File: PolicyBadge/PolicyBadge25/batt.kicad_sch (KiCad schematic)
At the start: 6 parts, among them U2 SGM40567-4.2XG/TR

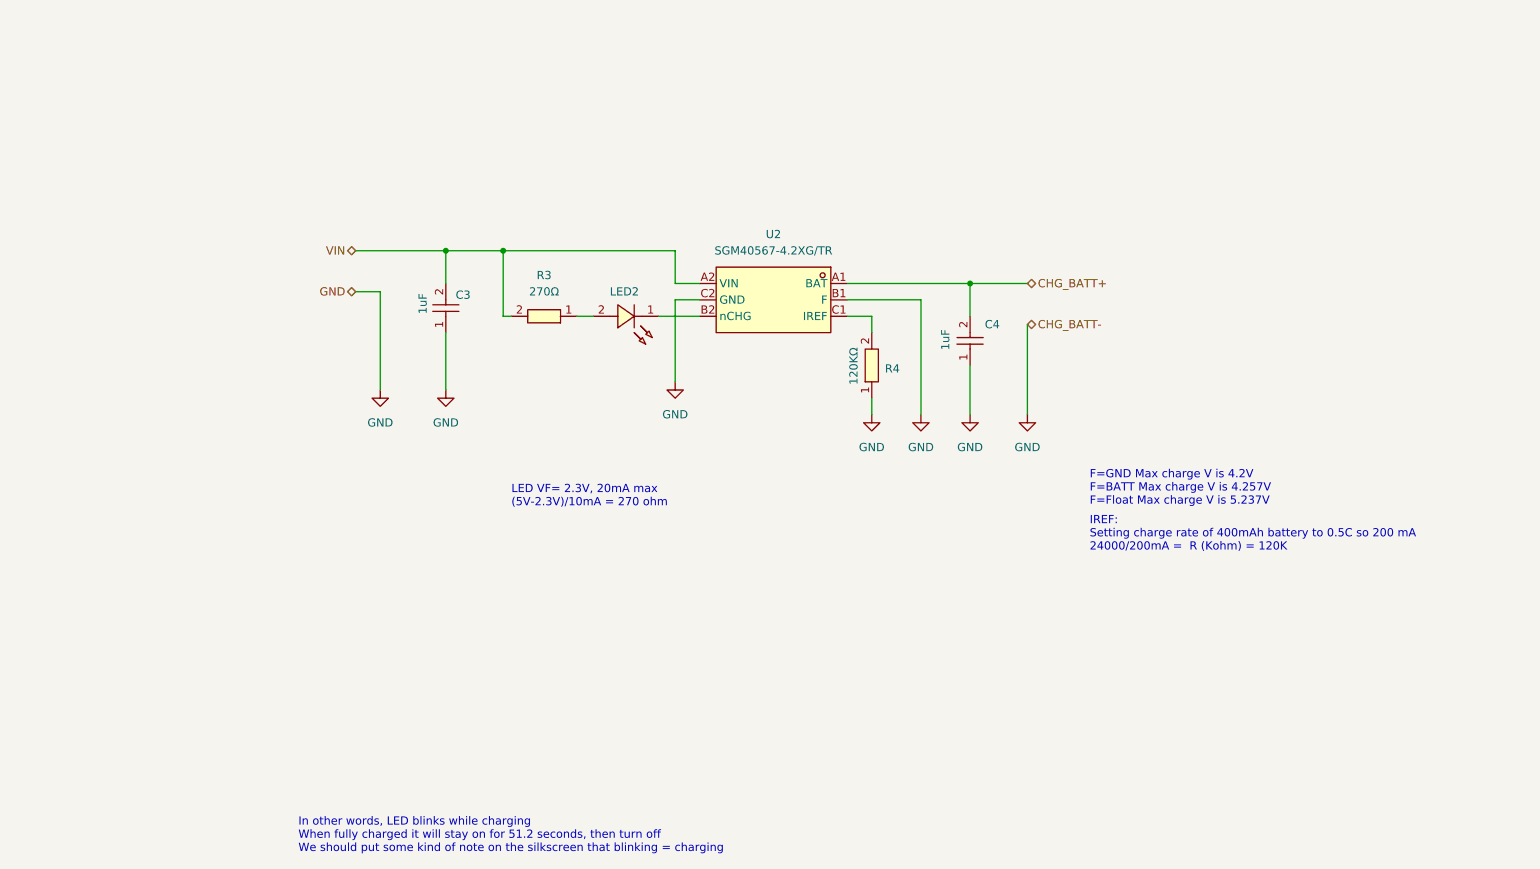
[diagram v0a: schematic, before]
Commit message: Use IP2312 battery management ic
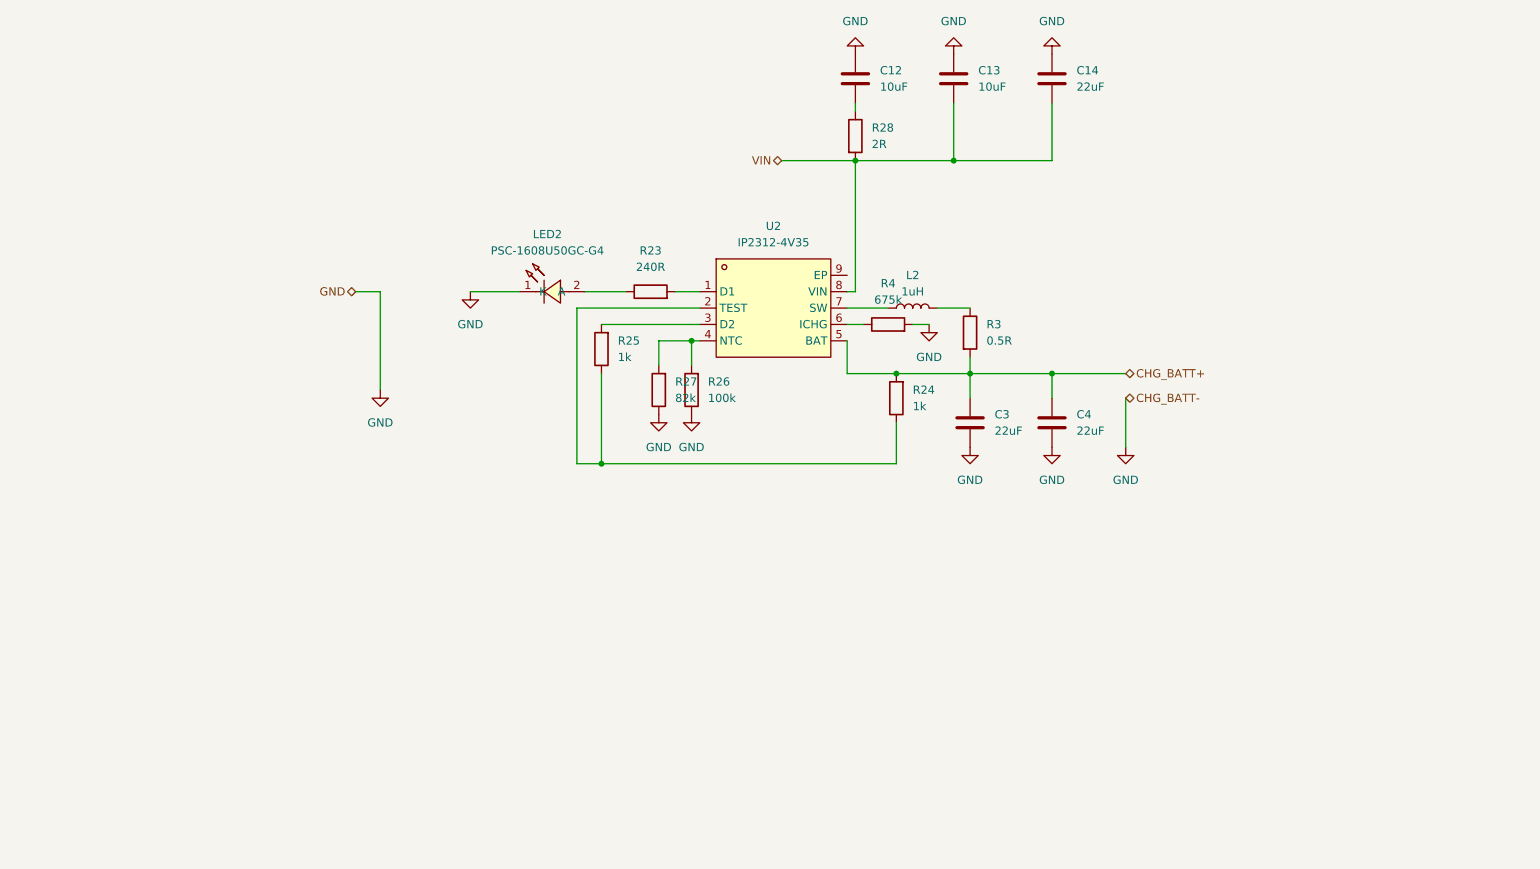
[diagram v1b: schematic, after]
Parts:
- removed C3, C4: 1uF, imported:C0603, symbol JLCPCB:CL10A105KO8NNNC
- removed LED2: ~, imported:LED0603-RD_RED, symbol JLCPCB:XL-1608SURC-06
- removed R3: 270Ω, imported:R0603, symbol JLCPCB:0603WAF2700T5E
- removed R4: 120KΩ, imported:R0603, symbol JLCPCB:0603WAF1203T5E
- removed U2: SGM40567-4.2XG/TR, imported:WLCSP-6_L1.2-W0.9-R3-C2-P0.40-TL, symbol JLCPCB:SGM40567-4.2XG_TR
- added C12, C13: 10uF, symbol Device:C
- added C14, C3, C4: 22uF, symbol Device:C
- added L2: 1uH, symbol Device:L
- added LED2: PSC-1608U50GC-G4, easyeda2kicad:LED0603-RD_GREEN, symbol easyeda2kicad:PSC-1608U50GC-G4
- added R23: 240R, symbol Device:R
- added R24, R25: 1k, symbol Device:R
- added R26: 100k, symbol Device:R
- added R27: 82k, symbol Device:R
- added R28: 2R, symbol Device:R
- added R3: 0.5R, symbol Device:R
- added R4: 675k, symbol Device:R
- added U2: IP2312-4V35, easyeda2kicad:ESOP-8_L4.9-W3.9-P1.27-LS6.0-BL-EP, symbol easyeda2kicad:IP2312-4V35
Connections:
- net CHG_BATT+: now also C3.1, C4.1, R24.2, R3.2, U2.5 (BAT)
- net GND: now also C12.1, C13.1, C14.1, C3.2, C4.2, LED2.1 (K), R26.1, R27.1, R4.2
- net VIN: now also C13.2, C14.2, R28.2, U2.8 (VIN)
- new net: R23.2, U2.1 (D1)
- new net: R24.1, R25.1, U2.2 (TEST)
- new net: R25.2, U2.3 (D2)
- new net: R26.2, R27.2, U2.4 (NTC)
- new net: R4.1, U2.6 (ICHG)
- new net: L2.1, U2.7 (SW)
- new net: LED2.2 (A), R23.1
- new net: C12.2, R28.1
- new net: L2.2, R3.1
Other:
- note removed: "F=GND Max charge V is 4.2V F=BATT Max charge V is 4.257V F=Float Max charge V is 5.237V"
- note removed: "IREF: Setting charge rate of 400mAh battery to 0.5C so 200 mA 24000/200mA = R (Kohm) = 120K"
- note removed: "In other words, LED blinks while charging When fully charged it will stay on for 51.2 seconds, then turn off We should put some kind of note on the silkscreen that blinking = charging"
- note removed: "LED VF= 2.3V, 20mA max (5V-2.3V)/10mA = 270 ohm"

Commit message: Released version of PCB
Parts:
- removed C12, C13: 10uF, symbol Device:C
- removed C14, C3, C4: 22uF, symbol Device:C
- removed L2: 1uH, symbol Device:L
- removed LED2: PSC-1608U50GC-G4, easyeda2kicad:LED0603-RD_GREEN, symbol easyeda2kicad:PSC-1608U50GC-G4
- removed R23: 240R, symbol Device:R
- removed R24, R25: 1k, symbol Device:R
- removed R26: 100k, symbol Device:R
- removed R27: 82k, symbol Device:R
- removed R28: 2R, symbol Device:R
- removed R3: 0.5R, symbol Device:R
- removed R4: 675k, symbol Device:R
- removed U2: IP2312-4V35, easyeda2kicad:ESOP-8_L4.9-W3.9-P1.27-LS6.0-BL-EP, symbol easyeda2kicad:IP2312-4V35
- added C13, C14: 10uF, imported:C0603, symbol JLCPCB:GRM188R6YA106MA73D
- added C15, C16, C17: 22uF, imported:C0805, symbol JLCPCB:CL21A226MAYNNNE
- added L2: 1uH, imported:L2520, symbol JLCPCB:DFE252012F-1R0M=P2
- added LED5: ~, imported:LED0603-RD_GREEN, symbol JLCPCB:PSC-1608U50GC-G4
- added R10: 51kΩ, imported:R0603, symbol JLCPCB:0603WAF5102T5E
- added R11: 680kΩ, imported:R0603, symbol JLCPCB:0603WAF6803T5E
- added R12: 0.5Ω, imported:R0603, symbol JLCPCB:0603WAF500LT5E
- added R7: 240Ω, imported:R0603, symbol JLCPCB:0603WAF2400T5E
- added R8, R9: 1KΩ, imported:R0603, symbol JLCPCB:0603WAF1001T5E
- added U11: IP2312-4V35, imported:ESOP-8_L4.9-W3.9-P1.27-LS6.0-BL-EP, symbol JLCPCB:IP2312-4V35
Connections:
- net CHG_BATT+: now also C17.2, L2.2, R12.2, R8.1, R9.2
- net GND: now also C13.1, C14.1, C15.1, C16.1, C17.1, LED5.1 (K), R10.1, R11.1, U11.9 (EP)
- net VIN: now also C13.2, C14.2, C15.2, U11.8 (VIN)
- new net: R10.2, U11.4 (NTC)
- new net: C16.2, R12.1, U11.5 (BAT)
- new net: R11.2, U11.6 (ICHG)
- new net: R8.2, U11.3 (D2)
- new net: L2.1, U11.7 (SW)
- new net: R9.1, U11.2 (TEST)
- new net: LED5.2 (A), R7.1
- new net: R7.2, U11.1 (D1)
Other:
- note added: "Battery type set to LiPoly with 4.2V by not connecting an RVSET resistor"
- note added: "ICHG resistor set to: 135000/680000 = 199 mA"
- note added: "One light mode configured"

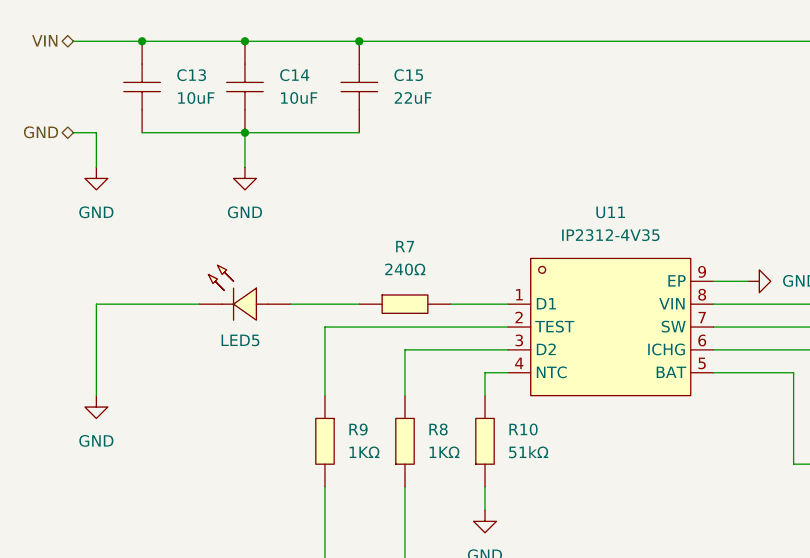
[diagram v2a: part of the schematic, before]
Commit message: Added batt monitoring
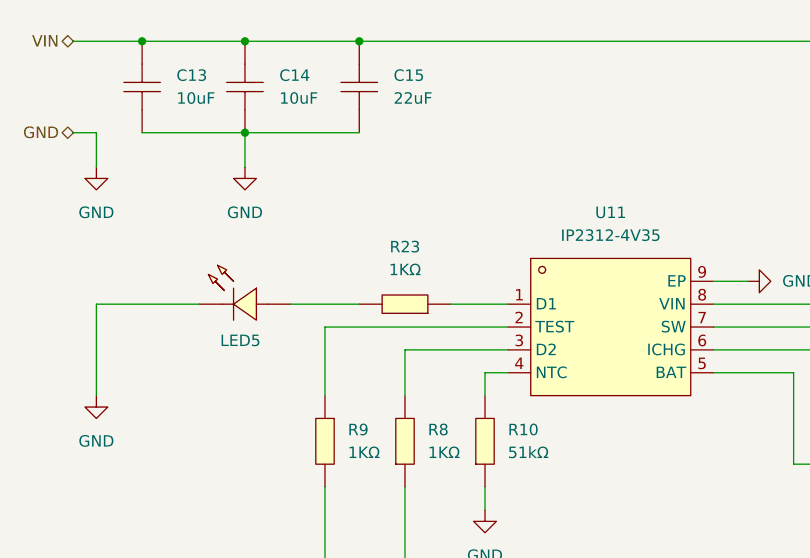
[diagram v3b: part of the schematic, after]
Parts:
- removed R7: 240Ω, imported:R0603, symbol JLCPCB:0603WAF2400T5E
- added R23: 1KΩ, imported:R0603, symbol JLCPCB:0603WAF1001T5E
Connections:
- net at LED5.2 (A): now also R23.2
- net at U11.1 (D1): now also R23.1
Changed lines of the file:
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@@
+	)
+	(symbol
+		(lib_id "JLCPCB:0603WAF1001T5E")
+		(at 115.57 86.36 180)
+		(unit 1)
+		(exclude_from_sim no)
+		(in_bom yes)
+		(on_board yes)
+		(dnp no)
+		(fields_autoplaced yes)
+		(property "Reference" "R23"
+			(at 115.57 80.01 0)
+			(effects
+				(font
+					(size 1.27 1.27)
+				)
+			)
+		)
+		(property "Value" "1KΩ"
+			(at 115.57 82.55 0)
+			(effects
+				(font
+					(size 1.27 1.27)
+				)
+			)
+		)
+		(property "Footprint" "imported:R0603"
+			(at 115.57 78.74 0)
+			(effects
+				(font
+					(size 1.27 1.27)
+				)
+				(hide yes)
+			)
+		)
+		(property "Datasheet" "https://lcsc.com/product-detail/Chip-Resistor-Surface-Mount-UniOhm_1KR-1001-1_C21190.html"
+			(at 115.57 76.2 0)
+			(effects
+				(font
+					(size 1.27 1.27)
+				)
+				(hide yes)
+			)
+		)
+		(property "Description" ""
+			(at 115.57 86.36 0)
+			(effects
+				(font
+					(size 1.27 1.27)
+				)
+				(hide yes)
+			)
+		)
+		(property "LCSC Part" "C21190"
+			(at 115.57 73.66 0)
+			(effects
+				(font
+					(size 1.27 1.27)
+				)
+				(hide yes)
+			)
+		)
+		(property "MPN" "0603WAF1001T5E"
+			(at 115.57 86.36 0)
+			(effects
+				(font
+					(size 1.27 1.27)
+				)
+				(hide yes)
+			)
+		)
+		(pin "2"
+		)
+		(pin "1"
+		)
+		(instances
+			(project "PolicyBadge25"
+				(path "/3911717a-8f19-42c2-8f04-ebfae4e12db6/9ee4cd69-77a2-45d3-80ac-b404a76d79db"
+					(reference "R23")
+					(unit 1)
+				)
+			)
+		)
 	)
 	(symbol
@@
 					(unit 1)
 				)
-			)
-		)
-	)
-	(symbol
-		(lib_id "JLCPCB:0603WAF2400T5E")
-		(at 115.57 86.36 0)
-		(unit 1)
-		(exclude_from_sim no)
-		(in_bom yes)
-		(on_board yes)
-		(dnp no)
-		(fields_autoplaced yes)
-		(property "Reference" "R7"
-			(at 115.57 80.01 0)
-			(effects
-				(font
-					(size 1.27 1.27)
-				)
-			)
-		)
-		(property "Value" "240Ω"
-			(at 115.57 82.55 0)
-			(effects
-				(font
-					(size 1.27 1.27)
-				)
-			)
-		)
-		(property "Footprint" "imported:R0603"
-			(at 115.57 93.98 0)
-			(effects
-				(font
-					(size 1.27 1.27)
-				)
-				(hide yes)
-			)
-		)
-		(property "Datasheet" "https://lcsc.com/product-detail/Chip-Resistor-Surface-Mount-UniOhm_240R-2400-1_C23350.html"
-			(at 115.57 96.52 0)
-			(effects
-				(font
-					(size 1.27 1.27)
-				)
-				(hide yes)
-			)
-		)
-		(property "Description" ""
-			(at 115.57 86.36 0)
-			(effects
-				(font
-					(size 1.27 1.27)
-				)
-				(hide yes)
-			)
-		)
-		(property "LCSC Part" "C23350"
-			(at 115.57 99.06 0)
-			(effects
-				(font
-					(size 1.27 1.27)
-				)
-				(hide yes)
-			)
-		)
-		(property "MPN" "0603WAF2400T5E"
-			(at 115.57 86.36 0)
-			(effects
-				(font
-					(size 1.27 1.27)
-				)
-				(hide yes)
-			)
-		)
-		(pin "2"
-		)
-		(pin "1"
-		)
-		(instances
-			(project "PolicyBadge25"
-				(path "/3911717a-8f19-42c2-8f04-ebfae4e12db6/9ee4cd69-77a2-45d3-80ac-b404a76d79db"
-					(reference "R7")
-					(unit 1)
-				)

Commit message: Lots of changes, laying out board for board shape
Updated switches
Added headers for XAIO
Fixed Batt Connector polarity
10K pullup on int
Batt monitor resistor divider
Fix buzzer trace
XAIO footprint spacing
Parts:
- renumbered C15 to C1, C13 to C2, C14 to C3, C16 to C4, C17 to C5, L2 to L1, LED5 to LED1, R9 to R7, R23 to R8, R8 to R9, U11 to U5
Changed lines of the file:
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@@
 		(dnp no)
 		(fields_autoplaced yes)
-		(property "Reference" "C14"
+		(property "Reference" "C3"
 			(at 101.6 60.9599 90)
 			(effects
@@
 			(project "PolicyBadge25"
 				(path "/3911717a-8f19-42c2-8f04-ebfae4e12db6/9ee4cd69-77a2-45d3-80ac-b404a76d79db"
-					(reference "C14")
+					(reference "C3")
 					(unit 1)
 				)
@@
 		(dnp no)
 		(fields_autoplaced yes)
-		(property "Reference" "#PWR021"
+		(property "Reference" "#PWR031"
 			(at 236.22 109.22 0)
 			(effects
@@
 			(project "PolicyBadge25"
 				(path "/3911717a-8f19-42c2-8f04-ebfae4e12db6/9ee4cd69-77a2-45d3-80ac-b404a76d79db"
-					(reference "#PWR021")
+					(reference "#PWR031")
 					(unit 1)
 				)
@@
 		(dnp no)
 		(fields_autoplaced yes)
-		(property "Reference" "#PWR023"
+		(property "Reference" "#PWR027"
 			(at 160.02 83.82 0)
 			(effects
@@
 			(project "PolicyBadge25"
 				(path "/3911717a-8f19-42c2-8f04-ebfae4e12db6/9ee4cd69-77a2-45d3-80ac-b404a76d79db"
-					(reference "#PWR023")
+					(reference "#PWR027")
 					(unit 1)
 				)
@@
 		(dnp no)
 		(fields_autoplaced yes)
-		(property "Reference" "#PWR063"
+		(property "Reference" "#PWR030"
 			(at 218.44 109.22 0)
 			(effects
@@
 			(project "PolicyBadge25"
 				(path "/3911717a-8f19-42c2-8f04-ebfae4e12db6/9ee4cd69-77a2-45d3-80ac-b404a76d79db"
-					(reference "#PWR063")
+					(reference "#PWR030")
 					(unit 1)
 				)
@@
 		(dnp no)
 		(fields_autoplaced yes)
-		(property "Reference" "R8"
+		(property "Reference" "R9"
 			(at 118.11 100.3299 90)
 			(effects
@@
 			(project ""
 				(path "/3911717a-8f19-42c2-8f04-ebfae4e12db6/9ee4cd69-77a2-45d3-80ac-b404a76d79db"
-					(reference "R8")
+					(reference "R9")
 					(unit 1)
 				)
@@
 		(dnp no)
 		(fields_autoplaced yes)
-		(property "Reference" "C17"
+		(property "Reference" "C5"
 			(at 222.25 96.5199 90)
 			(effects
@@
 			(project "PolicyBadge25"
 				(path "/3911717a-8f19-42c2-8f04-ebfae4e12db6/9ee4cd69-77a2-45d3-80ac-b404a76d79db"
-					(reference "C17")
+					(reference "C5")
 					(unit 1)
 				)
@@
 		(dnp no)
 		(fields_autoplaced yes)
-		(property "Reference" "L2"
+		(property "Reference" "L1"
 			(at 182.88 83.82 0)
 			(effects
@@
 			(project ""
 				(path "/3911717a-8f19-42c2-8f04-ebfae4e12db6/9ee4cd69-77a2-45d3-80ac-b404a76d79db"
-					(reference "L2")
+					(reference "L1")
 					(unit 1)
 				)
@@
 		(dnp no)
 		(fields_autoplaced yes)
-		(property "Reference" "#PWR058"
+		(property "Reference" "#PWR025"
 			(at 97.79 77.47 0)
 			(effects
@@
 			(project "PolicyBadge25"
 				(path "/3911717a-8f19-42c2-8f04-ebfae4e12db6/9ee4cd69-77a2-45d3-80ac-b404a76d79db"
-					(reference "#PWR058")
+					(reference "#PWR025")
 					(unit 1)
 				)
@@
 		(dnp no)
 		(fields_autoplaced yes)
-		(property "Reference" "R9"
+		(property "Reference" "R7"
 			(at 109.22 100.3299 90)
 			(effects
@@
 			(project "PolicyBadge25"
 				(path "/3911717a-8f19-42c2-8f04-ebfae4e12db6/9ee4cd69-77a2-45d3-80ac-b404a76d79db"
-					(reference "R9")
+					(reference "R7")
 					(unit 1)
 				)
@@
 		(on_board yes)
 		(dnp no)
-		(property "Reference" "LED5"
+		(property "Reference" "LED1"
 			(at 97.282 90.424 0)
 			(effects
@@
 			(project "PolicyBadge25"
 				(path "/3911717a-8f19-42c2-8f04-ebfae4e12db6/9ee4cd69-77a2-45d3-80ac-b404a76d79db"
-					(reference "LED5")
+					(reference "LED1")
 					(unit 1)
 				)
@@
 		(dnp no)
 		(fields_autoplaced yes)
-		(property "Reference" "R23"
+		(property "Reference" "R8"
 			(at 115.57 80.01 0)
 			(effects
@@
 			(project "PolicyBadge25"
 				(path "/3911717a-8f19-42c2-8f04-ebfae4e12db6/9ee4cd69-77a2-45d3-80ac-b404a76d79db"
-					(reference "R23")
+					(reference "R8")
 					(unit 1)
 				)
@@
 		(dnp no)
 		(fields_autoplaced yes)
-		(property "Reference" "#PWR062"
+		(property "Reference" "#PWR029"
 			(at 190.5 123.19 0)
 			(effects
@@
 			(project "PolicyBadge25"
 				(path "/3911717a-8f19-42c2-8f04-ebfae4e12db6/9ee4cd69-77a2-45d3-80ac-b404a76d79db"
-					(reference "#PWR062")
+					(reference "#PWR029")
 					(unit 1)
 				)
@@
 		(dnp no)
 		(fields_autoplaced yes)
-		(property "Reference" "C13"
+		(property "Reference" "C2"
 			(at 90.17 60.9599 90)
 			(effects
@@
 			(project "PolicyBadge25"
 				(path "/3911717a-8f19-42c2-8f04-ebfae4e12db6/9ee4cd69-77a2-45d3-80ac-b404a76d79db"
-					(reference "C13")
+					(reference "C2")
 					(unit 1)
 				)
@@
 		(dnp no)
 		(fields_autoplaced yes)
-		(property "Reference" "#PWR060"
+		(property "Reference" "#PWR026"
 			(at 124.46 115.57 0)
 			(effects
@@
 			(project "PolicyBadge25"
 				(path "/3911717a-8f19-42c2-8f04-ebfae4e12db6/9ee4cd69-77a2-45d3-80ac-b404a76d79db"
-					(reference "#PWR060")
+					(reference "#PWR026")
 					(unit 1)
 				)
@@
 		(dnp no)
 		(fields_autoplaced yes)
-		(property "Reference" "#PWR061"
+		(property "Reference" "#PWR028"
 			(at 177.8 99.06 0)
 			(effects
@@
 			(project "PolicyBadge25"
 				(path "/3911717a-8f19-42c2-8f04-ebfae4e12db6/9ee4cd69-77a2-45d3-80ac-b404a76d79db"
-					(reference "#PWR061")
+					(reference "#PWR028")
 					(unit 1)
 				)
@@
 		(dnp no)
 		(fields_autoplaced yes)
-		(property "Reference" "#PWR020"
+		(property "Reference" "#PWR023"
 			(at 81.28 77.47 0)
 			(effects
@@
 			(project "PolicyBadge25"
 				(path "/3911717a-8f19-42c2-8f04-ebfae4e12db6/9ee4cd69-77a2-45d3-80ac-b404a76d79db"
-					(reference "#PWR020")
+					(reference "#PWR023")
 					(unit 1)
 				)
@@
 		(dnp no)
 		(fields_autoplaced yes)
-		(property "Reference" "C16"
+		(property "Reference" "C4"
 			(at 194.31 110.4899 90)
 			(effects
@@
 			(project "PolicyBadge25"
 				(path "/3911717a-8f19-42c2-8f04-ebfae4e12db6/9ee4cd69-77a2-45d3-80ac-b404a76d79db"
-					(reference "C16")
+					(reference "C4")
 					(unit 1)
 				)
@@
 		(dnp no)
 		(fields_autoplaced yes)
-		(property "Reference" "C15"
+		(property "Reference" "C1"
 			(at 114.3 60.9599 90)
 			(effects
@@
 			(project ""
 				(path "/3911717a-8f19-42c2-8f04-ebfae4e12db6/9ee4cd69-77a2-45d3-80ac-b404a76d79db"
-					(reference "C15")
+					(reference "C1")
 					(unit 1)
 				)
@@
 		(dnp no)
 		(fields_autoplaced yes)
-		(property "Reference" "U11"
+		(property "Reference" "U5"
 			(at 138.43 76.2 0)
 			(effects
@@
 			(project ""
 				(path "/3911717a-8f19-42c2-8f04-ebfae4e12db6/9ee4cd69-77a2-45d3-80ac-b404a76d79db"
-					(reference "U11")
+					(reference "U5")
 					(unit 1)
 				)
@@
 		(dnp no)
 		(fields_autoplaced yes)
-		(property "Reference" "#PWR059"
+		(property "Reference" "#PWR024"
 			(at 81.28 102.87 0)
 			(effects
@@
 			(project "PolicyBadge25"
 				(path "/3911717a-8f19-42c2-8f04-ebfae4e12db6/9ee4cd69-77a2-45d3-80ac-b404a76d79db"
-					(reference "#PWR059")
-					(unit 1)
-				)
+					(reference "#PWR024")
+					(unit 1)
+				)
